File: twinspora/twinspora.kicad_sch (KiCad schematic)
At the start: 0 parts

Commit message: chip add
remaining components:
C5447274 -- DRV8316CRRGFR
C5155979 -- CA-IF1044VD-Q1
C19077434 -- BZT52B5V1S
C22459526 -- TS1187A26020
C2875244 -- CJ15-160000810A20
C96151 -- PRS3015-470MT
C2286 -- KT-0603R
C2290 -- KT-0603W
C165948 -- TYPE-C-31-M-12
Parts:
- added D1: 1N4148WS, Diode_SMD:D_SOD-323, symbol Diode:1N4148WS
- added Q1: AO3401A, Package_TO_SOT_SMD:SOT-23, symbol Transistor_FET:AO3401A
- added U1: STM32G473RBTx, Package_QFP:LQFP-64_10x10mm_P0.5mm, symbol MCU_ST_STM32G4:STM32G473RBTx
- added U2: MT6701QT, Package_DFN_QFN:QFN-16-1EP_3x3mm_P0.5mm_EP1.7x1.7mm, symbol Sensor_Magnetic:MT6701QT
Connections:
- new net: U1.15 (VSS), U1.31 (VSS), U1.47 (VSS), U1.63 (VSS)
- new net: U2.16 (GND), U2.17 (GND)

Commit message: g473 labels
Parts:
- added U3: MT6701QT, Package_DFN_QFN:QFN-16-1EP_3x3mm_P0.5mm_EP1.7x1.7mm, symbol Sensor_Magnetic:MT6701QT
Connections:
- net TIM1_CH3: now reaches U1.10 (PC2)
- net ADC2_IN9: now reaches U1.11 (PC3)
- net ADC2_IN1: now reaches U1.12 (PA0)
- net ADC1_IN2: now reaches U1.13 (PA1)
- net ADC1_IN3: now reaches U1.14 (PA2)
- net SPI1_NSS: now reaches U1.18 (PA4)
- net SPI1_SCK: now reaches U1.19 (PA5)
- net TIM1_CH1N: now reaches U1.2 (PC13)
- net SPI1_MISO: now reaches U1.20 (PA6)
- net SPI1_MOSI: now reaches U1.21 (PA7)
- net SPI4_MISO: now reaches U1.24 (PB0)
- net SPI4_MOSI: now reaches U1.25 (PB1)
- net SPI4_SCK: now reaches U1.30 (PB10)
- net SPI4_NSS: now reaches U1.33 (PB11)
- net FDCAN_RX: now reaches U1.34 (PB12)
- net SPI2_SCK: now reaches U1.35 (PB13)
- net TIM1_CH2N: now reaches U1.36 (PB14)
- net SPI2_MOSI: now reaches U1.37 (PB15)
- net TIM8_CH1: now reaches U1.38 (PC6)
- net TIM8_CH2: now reaches U1.39 (PC7)
- net TIM8_CH3: now reaches U1.40 (PC8)
- net SPI2_NSS: now reaches U1.41 (PC9)
- net ADC5_IN1: now reaches U1.42 (PA8)
- net ADC5_IN2: now reaches U1.43 (PA9)
- net SPI2_MISO: now reaches U1.44 (PA10)
- net D-: now reaches U1.45 (PA11)
- net D+: now reaches U1.46 (PA12)
- net SYS_SWDIO: now reaches U1.49 (PA13)
- net RCC_OSC_IN: now reaches U1.5 (PF0)
- net SYS_SWCLK: now reaches U1.50 (PA14)
- net I2C_SCL: now reaches U1.51 (PA15)
- net SPI3_SCK: now reaches U1.52 (PC10)
- net SPI3_MISO: now reaches U1.53 (PC11)
- net SPI3_MOSI: now reaches U1.54 (PC12)
- net SPI3_NSS: now reaches U1.55 (PD2)
- net TIM8_CH1N: now reaches U1.56 (PB3)
- net TIM8_CH2N: now reaches U1.57 (PB4)
- net TIM8_CH3N: now reaches U1.58 (PB5)
- net FDCAN_TX: now reaches U1.59 (PB6)
- net RCC_OSC_OUT: now reaches U1.6 (PF1)
- net I2C_SDA: now reaches U1.60 (PB7)
- net TIM1_CH3N: now reaches U1.62 (PB9)
- net TIM1_CH1: now reaches U1.8 (PC0)
- net TIM1_CH2: now reaches U1.9 (PC1)
- net at Q1.2 (S): now also D1.1 (K)
- net +3.3V: now reaches U2.13 (VDD)
- net +3.3V: now also U3.13 (VDD)
- net GND: now reaches U2.16 (GND), U2.17 (GND)
- net GND: now also U3.16 (GND), U3.17 (GND)
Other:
- moved on the sheet: D1, Q1, U1, U2

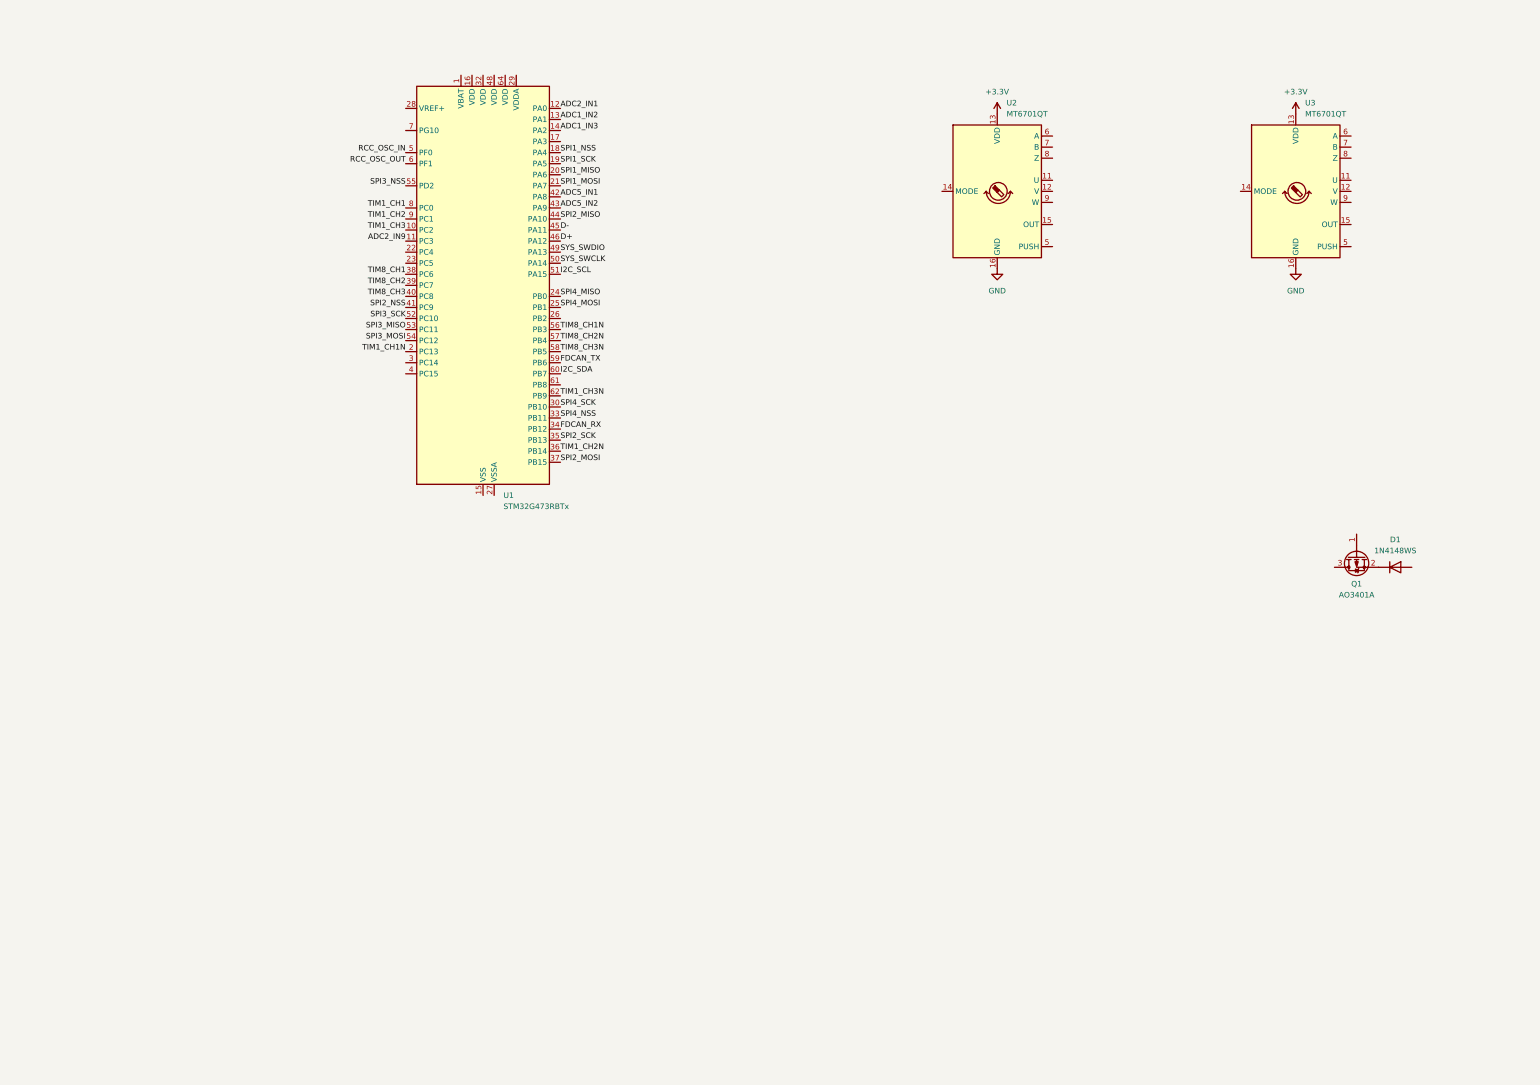
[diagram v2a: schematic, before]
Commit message: schematic and library work
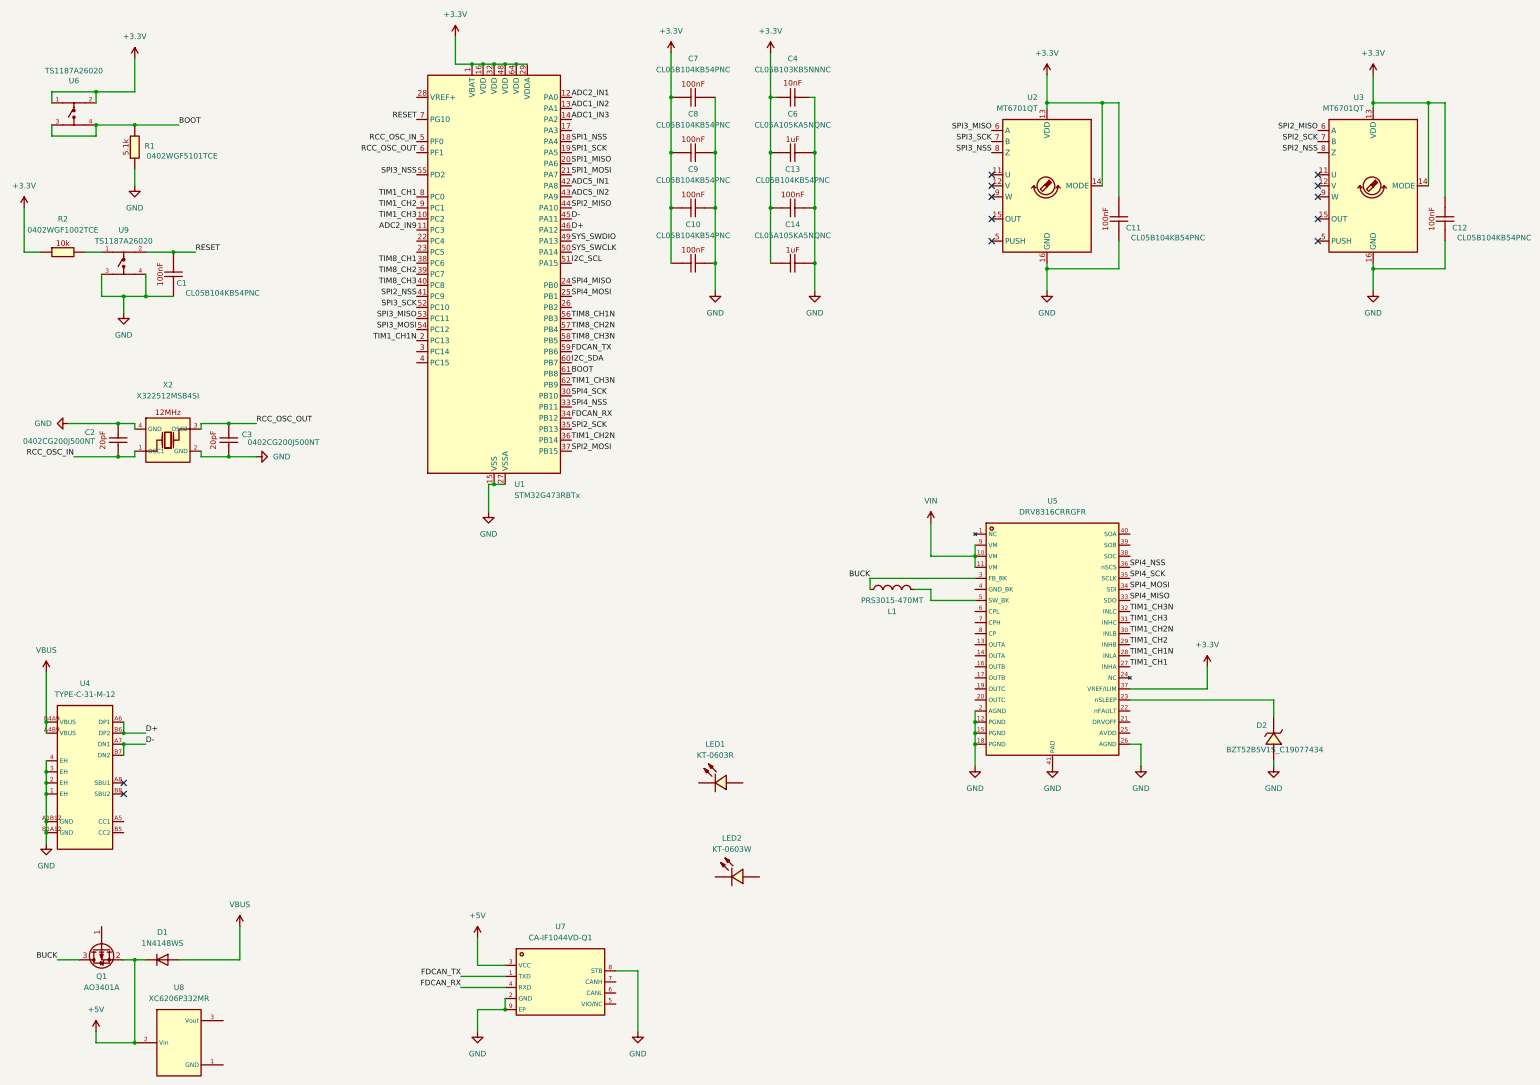
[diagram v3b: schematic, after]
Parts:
- added C1, C10, C11, C12, C13, C7, C8, C9: CL05B104KB54PNC, footprints/Basic_Capacitors_Resistors:C0402, symbol Basic_Capacitors_Resistors:CL05B104KB54PNC
- added C14, C6: CL05A105KA5NQNC, footprints/Basic_Capacitors_Resistors:C0402, symbol Basic_Capacitors_Resistors:CL05A105KA5NQNC
- added C2, C3: 0402CG200J500NT, footprints/Basic_Capacitors_Resistors:C0402, symbol Basic_Capacitors_Resistors:0402CG200J500NT
- added C4: CL05B103KB5NNNC, footprints/Basic_Capacitors_Resistors:C0402, symbol Basic_Capacitors_Resistors:CL05B103KB5NNNC
- added D2: BZT52B5V1S_C19077434, footprints/Diode:SOD-323_L1.7-W1.3-LS2.6-RD, symbol Diode:BZT52B5V1S_C19077434
- added L1: PRS3015-470MT, footprints/Inductor:IND-SMD_L3.0-W3.0_PRS3015, symbol Inductor:PRS3015-470MT
- added LED1: KT-0603R, footprints/LED:LED0603-RD, symbol LED:KT-0603R
- added LED2: KT-0603W, footprints/LED:LED0603-R-RD_WHITE, symbol LED:KT-0603W
- added R1: 0402WGF5101TCE, footprints/Basic_Capacitors_Resistors:R0402, symbol Basic_Capacitors_Resistors:0402WGF5101TCE
- added R2: 0402WGF1002TCE, footprints/Basic_Capacitors_Resistors:R0402, symbol Basic_Capacitors_Resistors:0402WGF1002TCE
- added U4: TYPE-C-31-M-12, footprints/Connector_USB:USB-C_SMD-TYPE-C-31-M-12_1, symbol Connector_USB:TYPE-C-31-M-12
- added U5: DRV8316CRRGFR, footprints/Motor_Driver:VQFN-40_L7.0-W5.0-P0.50-BL-EP5.7, symbol Motor_Driver:DRV8316CRRGFR
- added U6, U9: TS1187A26020, footprints/Switch:SW-SMD_4P-L5.2-W5.2-1, symbol Switch:TS1187A26020
- added U7: CA-IF1044VD-Q1, footprints/Interface_CAN_LIN:DFN-8_L3.0-W3.0-P0.65-BL-EP2.45, symbol Interface_CAN_LIN:CA-IF1044VD-Q1
- added U8: XC6206P332MR, footprints/Regulator_Linear:SOT-23-3_L2.9-W1.6-P1.90-LS2.8-BR, symbol Regulator_Linear:XC6206P332MR
- added X2: X322512MSB4SI, Device:X322512MSB4SI, symbol Oscillator:X322512MSB4SI
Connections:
- net +3.3V: now also U1.1 (VBAT), U1.16 (VDD), U1.29 (VDDA), U1.32 (VDD), U1.48 (VDD), U1.64 (VDD), U2.14 (MODE), U3.14 (MODE), C10.1, C11.2, C12.2, C13.1, C14.1, C4.1, C6.1, C7.1, C8.1, C9.1, R2.1, U5.37 (VREF/ILIM), U6.1, U6.2
- net D+: now also U4.A6 (DP1), U4.B6 (DP2)
- net D-: now also U4.A7 (DN1), U4.B7 (DN2)
- net FDCAN_RX: now also U7.4 (RXD)
- net FDCAN_TX: now also U7.1 (TXD)
- net GND: now also U1.15 (VSS), U1.27 (VSSA), U1.31 (VSS), U1.47 (VSS), U1.63 (VSS), C1.1, C10.2, C11.1, C12.1, C13.2, C14.2, C2.2, C3.1, C4.2, C6.2, C7.2, C8.2, C9.2, D2.2 (A), R1.1, U4.1 (EH), U4.2 (EH), U4.3 (EH), U4.4 (EH), U4.A1B12 (GND), U4.B1A12 (GND), U5.12 (PGND), U5.15 (PGND), U5.18 (PGND), U5.2 (AGND), U5.26 (AGND), U5.41 (PAD), U7.2 (GND), U7.8 (STB), U7.9 (EP), U9.3, U9.4, X2.2 (GND), X2.4 (GND)
- net RCC_OSC_IN: now also C2.1, X2.1 (OSC1)
- net RCC_OSC_OUT: now also C3.2, X2.3 (OSC2)
- net SPI2_MISO: now also U3.6 (A)
- net SPI2_NSS: now also U3.8 (Z)
- net SPI2_SCK: now also U3.7 (B)
- net SPI3_MISO: now also U2.6 (A)
- net SPI3_NSS: now also U2.8 (Z)
- net SPI3_SCK: now also U2.7 (B)
- net SPI4_MISO: now also U5.33 (SDO)
- net SPI4_MOSI: now also U5.34 (SDI)
- net SPI4_NSS: now also U5.36 (nSCS)
- net SPI4_SCK: now also U5.35 (SCLK)
- net TIM1_CH1: now also U5.27 (INHA)
- net TIM1_CH1N: now also U5.28 (INLA)
- net TIM1_CH2: now also U5.29 (INHB)
- net TIM1_CH2N: now also U5.30 (INLB)
- net TIM1_CH3: now also U5.31 (INHC)
- net TIM1_CH3N: now also U5.32 (INLC)
- net BOOT: now reaches U1.61 (PB8)
- net BOOT: now also R1.2, U6.3, U6.4
- net RESET: now reaches U1.7 (PG10)
- net RESET: now also C1.2, U9.2
- net +5V: now reaches D1.1 (K), Q1.2 (S)
- net +5V: now also U7.3 (VCC), U8.2 (Vin)
- net BUCK: now reaches Q1.3 (D)
- net BUCK: now also L1.2, U5.3 (FB_BK)
- net VBUS: now reaches D1.2 (A)
- net VBUS: now also U4.A4B9 (VBUS), U4.B4A9 (VBUS)
- new net: R2.2, U9.1
- new net: D2.1 (K), U5.23 (nSLEEP)
- new net: L1.1, U5.5 (SW_BK)
- new net VIN: U5.10 (VM), U5.11 (VM), U5.9 (VM)
- no-connect marks 0 -> 12
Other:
- moved on the sheet: D1, Q1, U1, U2

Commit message: finished schematic, added connectors
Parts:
- removed U4: TYPE-C-31-M-12, footprints/Connector_USB:USB-C_SMD-TYPE-C-31-M-12_1, symbol Connector_USB:TYPE-C-31-M-12
- added C15, C21, C22, C23, C25, C28, C29, C30, C34: CL10A226MQ8NRNC, footprints/Basic_Capacitors_Resistors:C0603, symbol Basic_Capacitors_Resistors:CL10A226MQ8NRNC
- added C16, C17, C18, C19, C26, C33: CL05B104KB54PNC, footprints/Basic_Capacitors_Resistors:C0402, symbol Basic_Capacitors_Resistors:CL05B104KB54PNC
- added C20, C24, C27, C31, C32: CL05A105KA5NQNC, footprints/Basic_Capacitors_Resistors:C0402, symbol Basic_Capacitors_Resistors:CL05A105KA5NQNC
- added C5: CL10A475KO8NNNC, footprints/Basic_Capacitors_Resistors:C0603, symbol Basic_Capacitors_Resistors:CL10A475KO8NNNC
- added D3: BZT52B5V1S_C19077434, footprints/Diode:SOD-323_L1.7-W1.3-LS2.6-RD, symbol Diode:BZT52B5V1S_C19077434
- added J1: XY-SH1_0-4A61, footprints/Connector_SH1.0:CONN-SMD_4P-P1.00-WT, symbol Connector_SH1.0:XY-SH1_0-4A61
- added J2: TYPE-C-31-M-12, footprints/Connector_USB:USB-C_SMD-TYPE-C-31-M-12_1, symbol Connector_USB:TYPE-C-31-M-12
- added J3, J4: XY-SH1_0-6A51, footprints/Connector_SH1.0:CONN-SMD_6P-P1.00_XY-SH1.0-6A51, symbol Connector_SH1.0:XY-SH1_0-6A51
- added J5, J6: XY-XH2_54-2A21, footprints/Connector_XH2.54:HDR-TH_2P-P2.50_XY-XH2.54-2A21, symbol Connector_XH2.54:XY-XH2_54-2A21
- added L2: PRS3015-470MT, footprints/Inductor:IND-SMD_L3.0-W3.0_PRS3015, symbol Inductor:PRS3015-470MT
- added R10, R3, R5: 0402WGF1002TCE, footprints/Basic_Capacitors_Resistors:R0402, symbol Basic_Capacitors_Resistors:0402WGF1002TCE
- added R11, R17, R20: 0402WGF1003TCE, footprints/Basic_Capacitors_Resistors:R0402, symbol Basic_Capacitors_Resistors:0402WGF1003TCE
- added R12, R13, R18, R22, R9: 0402WGF5101TCE, footprints/Basic_Capacitors_Resistors:R0402, symbol Basic_Capacitors_Resistors:0402WGF5101TCE
- added R14, R15, R16, R19, R21, R23, R6, R8: 0402WGF3300TCE, footprints/Basic_Capacitors_Resistors:R0402, symbol Basic_Capacitors_Resistors:0402WGF3300TCE
- added R4: 0402WGF1200TCE, footprints/Basic_Capacitors_Resistors:R0402, symbol Basic_Capacitors_Resistors:0402WGF1200TCE
- added U10: DRV8316CRRGFR, footprints/Motor_Driver:VQFN-40_L7.0-W5.0-P0.50-BL-EP5.7, symbol Motor_Driver:DRV8316CRRGFR
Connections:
- net +3.3V: now also U1.28 (VREF+), U8.3 (Vout), C15.2, C16.2, C5.1, J1.2, J3.2, J4.2, R18.2, R22.2, R9.1, U10.37 (VREF/ILIM)
- net +5V: now also C17.2, C19.2
- net ADC1_IN2: now also C23.2, R16.2
- net ADC1_IN3: now also C28.2, R19.2
- net ADC2_IN1: now also C22.2, R15.2
- net ADC2_IN9: now also C29.2, R21.2
- net ADC5_IN1: now also C21.2, R14.2
- net ADC5_IN2: now also C30.2, R23.2
- net BUCK: now also C25.2, C34.2, L2.2, U10.3 (FB_BK)
- net D+: now also J2.A6 (DP1), J2.B6 (DP2)
- net D-: now also J2.A7 (DN1), J2.B7 (DN2)
- net GND: now also LED1.1 (K), LED2.2 (K), U5.4 (GND_BK), U8.1 (GND), C15.1, C16.1, C17.1, C18.1, C19.1, C20.1, C21.1, C22.1, C23.1, C24.1, C25.1, C28.1, C29.1, C30.1, C31.1, C34.1, C5.2, D3.2 (A), J1.1, J1.5, J1.6, J2.1 (EH), J2.2 (EH), J2.3 (EH), J2.4 (EH), J2.A1B12 (GND), J2.B1A12 (GND), J3.1, J3.7, J3.8, J4.1, J4.7, J4.8, R10.1, R12.2, R13.2, R3.1, R5.1, U10.12 (PGND), U10.15 (PGND), U10.18 (PGND), U10.2 (AGND), U10.26 (AGND), U10.4 (GND_BK), U10.41 (PAD)
- net I2C_SCL: now also J1.4
- net I2C_SDA: now also J1.3
- net SPI1_MISO: now also U10.33 (SDO)
- net SPI1_MOSI: now also U10.34 (SDI)
- net SPI1_NSS: now also U10.36 (nSCS)
- net SPI1_SCK: now also U10.35 (SCLK)
- net SPI2_MISO: now also J4.5
- net SPI2_MOSI: now also J4.6
- net SPI2_NSS: now also J4.3
- net SPI2_SCK: now also J4.4
- net SPI3_MISO: now also J3.5
- net SPI3_MOSI: now also J3.6
- net SPI3_NSS: now also J3.3
- net SPI3_SCK: now also J3.4
- net TIM8_CH1: now also U10.27 (INHA)
- net TIM8_CH1N: now also U10.28 (INLA)
- net TIM8_CH2: now also U10.29 (INHB)
- net TIM8_CH2N: now also U10.30 (INLB)
- net TIM8_CH3: now also U10.31 (INHC)
- net TIM8_CH3N: now also U10.32 (INLC)
- net VBUS: now also J2.A4B9 (VBUS), J2.B4A9 (VBUS), R6.2
- net VIN: now also C27.2, C32.2, R11.2, R17.2, R20.2, U10.10 (VM), U10.11 (VM), U10.9 (VM)
- net at LED2.1 (A): now also R9.2
- net VSENS: now reaches U1.17 (PA3)
- net CAN_VIO: now reaches U1.22 (PC4)
- net CAN_VIO: now also U7.5 (VIO/NC), C18.2, R5.2
- net USER_LED: now reaches U1.23 (PC5)
- net USER_LED: now also R8.1
- net GPIO3: now reaches U1.26 (PB2)
- net GPIO1: now reaches U1.3 (PC14)
- net GPIO2: now reaches U1.4 (PC15)
- net at LED1.2 (A): now also R8.2
- net at Q1.1 (G): now also R3.2, R6.1
- net NSLEEP: now reaches D2.1 (K), U5.23 (nSLEEP)
- net NSLEEP: now also D3.1 (K), R17.1, R20.1, U10.23 (nSLEEP)
- net CAN_L: now reaches U7.6 (CANL)
- net CAN_L: now also J5.2, J6.2, R4.2
- net CAN_H: now reaches U7.7 (CANH)
- net CAN_H: now also J5.1, J6.1, R4.1
- net PHA1: now reaches U5.13 (OUTA)
- net PHA1: now also U5.14 (OUTA)
- net PHB1: now reaches U5.16 (OUTB)
- net PHB1: now also U5.17 (OUTB)
- net PHC1: now reaches U5.19 (OUTC)
- net PHC1: now also U5.20 (OUTC)
- net NFAULT: now reaches U5.22 (nFAULT)
- net NFAULT: now also R18.1, R22.1, U10.22 (nFAULT)
- net at U5.25 (AVDD): now also C24.2
- net at U5.38 (SOC): now also R14.1
- net at U5.39 (SOB): now also R15.1
- net at U5.40 (SOA): now also R16.1
- net at U5.6 (CPL): now also C26.2
- net at U5.7 (CPH): now also C26.1
- net at U5.8 (CP): now also C27.1
- new net: C31.2, U10.25 (AVDD)
- new net: R23.1, U10.38 (SOC)
- new net: C20.2, R10.2, R11.1
- new net: R19.1, U10.40 (SOA)
- new net: R21.1, U10.39 (SOB)
- new net: L2.1, U10.5 (SW_BK)
- new net: C33.2, U10.6 (CPL)
- new net: C33.1, U10.7 (CPH)
- new net: C32.1, U10.8 (CP)
- new net CC1: J2.A5 (CC1), R12.1
- new net CC2: J2.B5 (CC2), R13.1
- new net PHA2: U10.13 (OUTA), U10.14 (OUTA)
- new net PHB2: U10.16 (OUTB), U10.17 (OUTB)
- new net PHC2: U10.19 (OUTC), U10.20 (OUTC)
- no-connect marks 12 -> 18
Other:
- note added: "3.3V Regulator"
- note added: "Alternate Part: SIT1042ATK/3"
- note added: "Battery Voltage Sense"
- note added: "CAN Transciever - CA-IF1044VD-Q1"
- note added: "Encoder 1"
- note added: "Encoder 2"
- note added: "LED"
- note added: "MCU - STM32G473RBT6"
- note added: "Magnetic Encoder - MT6701QT"
- note added: "Motor Driver - DRV8316CR"
- note added: "Motor Driver 1"
- note added: "Motor Driver 2"
- note added: "USB 2.0"
- note added: "VDD Decoupling"
- note added: "VDDA/VREF Decoupling"
- note added: "Voltage Divider"
- title: (none) -> Twinspora
- moved on the sheet: C1, C10, C11, C12, C13, C14, C4, C6, C7, C8, C9, D1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

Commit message: new adc lpf values
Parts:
- removed C21, C22, C23, C28, C29, C30: CL10A226MQ8NRNC, footprints/Basic_Capacitors_Resistors:C0603, symbol Basic_Capacitors_Resistors:CL10A226MQ8NRNC
- removed R14, R15, R16, R19, R21, R23: 0402WGF3300TCE, footprints/Basic_Capacitors_Resistors:R0402, symbol Basic_Capacitors_Resistors:0402WGF3300TCE
- added C21, C22, C23, C28, C29, C30: CL05B103KB5NNNC, Basic_Capacitors_Resistors:C0402, symbol Basic_Capacitors_Resistors:CL05B103KB5NNNC
- added J7: XY-XH2_54-3A11, Connector_XH2.54:HDR-TH_3P-P2.50-V-F-2, symbol Connector_XH2.54:XY-XH2_54-3A11
- added R14, R15, R16, R19, R21, R7: 0402WGF499JTCE, Basic_Capacitors_Resistors:R0402, symbol Basic_Capacitors_Resistors:0402WGF499JTCE
- C1, C10, C11, C12, C13, C14, C16, C17, C18, C19, C2, C20, C24, C26, C27, C3, C31, C32, C33, C4, C6, C7, C8, C9: footprint footprints/Basic_Capacitors_Resistors:C0402 -> Basic_Capacitors_Resistors:C0402
- C15, C25, C34, C5: footprint footprints/Basic_Capacitors_Resistors:C0603 -> Basic_Capacitors_Resistors:C0603
- D2, D3: footprint footprints/Diode:SOD-323_L1.7-W1.3-LS2.6-RD -> Diode:SOD-323_L1.7-W1.3-LS2.6-RD
- J1: footprint footprints/Connector_SH1.0:CONN-SMD_4P-P1.00-WT -> Connector_SH1.0:CONN-SMD_4P-P1.00-WT
- J2: footprint footprints/Connector_USB:USB-C_SMD-TYPE-C-31-M-12_1 -> Connector_USB:USB-C_SMD-TYPE-C-31-M-12_1
- J3, J4: footprint footprints/Connector_SH1.0:CONN-SMD_6P-P1.00_XY-SH1.0-6A51 -> Connector_SH1.0:CONN-SMD_6P-P1.00_XY-SH1.0-6A51
- J5, J6: footprint footprints/Connector_XH2.54:HDR-TH_2P-P2.50_XY-XH2.54-2A21 -> Connector_XH2.54:HDR-TH_2P-P2.50_XY-XH2.54-2A21
- L1, L2: footprint footprints/Inductor:IND-SMD_L3.0-W3.0_PRS3015 -> Inductor:IND-SMD_L3.0-W3.0_PRS3015
- LED1: footprint footprints/LED:LED0603-RD -> LED:LED0603-RD
- LED2: footprint footprints/LED:LED0603-R-RD_WHITE -> LED:LED0603-R-RD_WHITE
- R1, R10, R11, R12, R13, R17, R18, R2, R20, R22, R3, R4, R5, R6, R8, R9: footprint footprints/Basic_Capacitors_Resistors:R0402 -> Basic_Capacitors_Resistors:R0402
- U10, U5: footprint footprints/Motor_Driver:VQFN-40_L7.0-W5.0-P0.50-BL-EP5.7 -> Motor_Driver:VQFN-40_L7.0-W5.0-P0.50-BL-EP5.7
- U6, U9: footprint footprints/Switch:SW-SMD_4P-L5.2-W5.2-1 -> Switch:SW-SMD_4P-L5.2-W5.2-1
- U7: footprint footprints/Interface_CAN_LIN:DFN-8_L3.0-W3.0-P0.65-BL-EP2.45 -> Interface_CAN_LIN:DFN-8_L3.0-W3.0-P0.65-BL-EP2.45
- U8: footprint footprints/Regulator_Linear:SOT-23-3_L2.9-W1.6-P1.90-LS2.8-BR -> Regulator_Linear:SOT-23-3_L2.9-W1.6-P1.90-LS2.8-BR
- X2: footprint Device:X322512MSB4SI -> Oscillator:X322512MSB4SI
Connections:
- net VIN is gone; now on net VBUS: C27.2, C32.2, R11.2, R17.2, R20.2, U10.10 (VM), U10.11 (VM), U10.9 (VM), U5.10 (VM), U5.11 (VM), U5.9 (VM)
- net +5V: no longer U7.3 (VCC)
- net ADC1_IN2: now also C21.2, R7.1
- net ADC1_IN3: now also C28.2, R21.1
- net ADC2_IN1: now also C22.2, R14.1
- net ADC2_IN9: now also C29.2, R19.1
- net ADC5_IN1: now also C23.2, R15.1
- net ADC5_IN2: now also C30.2, R16.1
- net FDCAN_RX: no longer U7.4 (RXD)
- net FDCAN_TX: no longer U7.1 (TXD)
- net GND: now also C21.1, C22.1, C23.1, C28.1, C29.1, C30.1; no longer U7.2 (GND), U7.9 (EP)
- net GPIO1: now also J7.1
- net GPIO2: now also J7.2
- net GPIO3: now also J7.3
- net at U10.38 (SOC): now also R16.2
- net at U5.39 (SOB): now also R14.2
- net at U10.40 (SOA): now also R21.2
- net at U5.40 (SOA): now also R7.2
- net at U5.38 (SOC): now also R15.2
- net at U10.39 (SOB): now also R19.2
- no-connect marks 18 -> 20
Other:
- note added: "GPIO Breakout (optional)"
